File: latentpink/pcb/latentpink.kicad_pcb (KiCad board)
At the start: 6 copper layers, 97 parts, among them J1 CONN_SFP_HOST, J2 SFP_CAGE, J3 RJ45, J4 RJ45, U1 VSC8512, U2 XC7K160T-2FBG484C, U3 CY7C2245KV18-450BZXI, U4 STM32H735-UFBGA176-25, U5 DP83867, U6 DP83867, U7 BEL_FUSE_S558-5999-M8-F, U8 BEL_FUSE_S558-5999-M8-F

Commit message: Continued initial schematic capture
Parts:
- added C106: 4.7 uF, azonenberg_pcb:EIA_0603_CAP_NOSILK, F.Cu at (205.3, 132.9)
- added C110: 0.47 uF, azonenberg_pcb:EIA_0402_CAP_NOSILK, F.Cu at (208.7, 137.6)
- added C111: 0.1 uF, azonenberg_pcb:EIA_0402_CAP_NOSILK, F.Cu at (211.2, 137.2)
- added C115: 0.47 uF, azonenberg_pcb:EIA_0402_CAP_NOSILK, F.Cu at (207.4, 136.1)
- added C116: 0.47 uF, azonenberg_pcb:EIA_0402_CAP_NOSILK, F.Cu at (207.4, 134.6)
- added C119: 0.47 uF, azonenberg_pcb:EIA_0402_CAP_NOSILK, F.Cu at (208.2, 132.8)
- added C121: 0.015 uF, azonenberg_pcb:EIA_0603_CAP_NOSILK, F.Cu at (60.0, 135.2)
- added C123: 0.47 uF, azonenberg_pcb:EIA_0402_CAP_NOSILK, F.Cu at (197.5, 139.8)
- added C124: 4.7 uF, azonenberg_pcb:EIA_0603_CAP_NOSILK, F.Cu at (22.1, 62.0)
- added C125: 4.7 uF, azonenberg_pcb:EIA_0603_CAP_NOSILK, F.Cu at (22.1, 60.2)
- added C126: 4.7 uF, azonenberg_pcb:EIA_0603_CAP_NOSILK, F.Cu at (22.1, 63.8)
- added C127: 4.7 uF, azonenberg_pcb:EIA_0603_CAP_NOSILK, F.Cu at (25.4, 60.2)
- added C128: 0.47 uF, azonenberg_pcb:EIA_0402_CAP_NOSILK, F.Cu at (21.7, 68.5)
- added C129: 0.47 uF, azonenberg_pcb:EIA_0402_CAP_NOSILK, B.Cu at (29.8, 72.8)
- added C130: 0.47 uF, azonenberg_pcb:EIA_0402_CAP_NOSILK, F.Cu at (21.7, 67.0)
- added C131: 0.47 uF, azonenberg_pcb:EIA_0402_CAP_NOSILK, B.Cu at (24.8, 75.8)
- added C132: 0.47 uF, azonenberg_pcb:EIA_0402_CAP_NOSILK, F.Cu at (24.2, 65.5)
- added C133: 0.47 uF, azonenberg_pcb:EIA_0402_CAP_NOSILK, F.Cu at (30.8, 60.0)
- added C134: 0.47 uF, azonenberg_pcb:EIA_0402_CAP_NOSILK, F.Cu at (25.0, 61.9)
- added C135: 0.47 uF, azonenberg_pcb:EIA_0402_CAP_NOSILK, F.Cu at (33.3, 60.0)
- added C136: 0.47 uF, azonenberg_pcb:EIA_0402_CAP_NOSILK, F.Cu at (25.0, 63.4)
- added C137: 0.47 uF, azonenberg_pcb:EIA_0402_CAP_NOSILK, B.Cu at (31.8, 75.8)
- added C138: 0.47 uF, azonenberg_pcb:EIA_0402_CAP_NOSILK, F.Cu at (21.7, 65.5)
- added C139: 0.47 uF, azonenberg_pcb:EIA_0402_CAP_NOSILK, B.Cu at (25.8, 72.8)
- added C140: 0.47 uF, azonenberg_pcb:EIA_0402_CAP_NOSILK, B.Cu at (26.8, 72.8)
- added C141: 0.47 uF, azonenberg_pcb:EIA_0402_CAP_NOSILK, B.Cu at (24.8, 71.8)
- added C142: 0.47 uF, azonenberg_pcb:EIA_0402_CAP_NOSILK, F.Cu at (24.2, 68.5)
- added C143: 0.47 uF, azonenberg_pcb:EIA_0402_CAP_NOSILK, F.Cu at (32.5, 61.5)
- added C144: 0.47 uF, azonenberg_pcb:EIA_0402_CAP_NOSILK, B.Cu at (30.8, 72.7)
- added C145: 0.47 uF, azonenberg_pcb:EIA_0402_CAP_NOSILK, B.Cu at (27.8, 72.8)
- added C146: 0.47 uF, azonenberg_pcb:EIA_0402_CAP_NOSILK, F.Cu at (27.5, 63.4)
- added C147: 0.47 uF, azonenberg_pcb:EIA_0402_CAP_NOSILK, F.Cu at (29.2, 66.3)
- added C148: 0.47 uF, azonenberg_pcb:EIA_0402_CAP_NOSILK, F.Cu at (26.7, 66.3)
- added C149: 0.47 uF, azonenberg_pcb:EIA_0402_CAP_NOSILK, F.Cu at (24.2, 67.0)
- added C150: 0.47 uF, azonenberg_pcb:EIA_0402_CAP_NOSILK, F.Cu at (28.3, 60.0)
- added C151: 0.47 uF, azonenberg_pcb:EIA_0402_CAP_NOSILK, F.Cu at (29.2, 64.8)
- added C152: 0.47 uF, azonenberg_pcb:EIA_0402_CAP_NOSILK, B.Cu at (31.8, 71.8)
- added C153: 0.47 uF, azonenberg_pcb:EIA_0402_CAP_NOSILK, F.Cu at (27.5, 61.9)
- added C162: 4.7 uF, azonenberg_pcb:EIA_0603_CAP_NOSILK, F.Cu at (21.8, 76.5)
- added C163: 4.7 uF, azonenberg_pcb:EIA_0603_CAP_NOSILK, F.Cu at (21.8, 74.7)
- added C164: 4.7 uF, azonenberg_pcb:EIA_0603_CAP_NOSILK, F.Cu at (25.1, 76.5)
- added C165: 4.7 uF, azonenberg_pcb:EIA_0603_CAP_NOSILK, F.Cu at (25.1, 74.7)
- added C166: 4.7 uF, azonenberg_pcb:EIA_0603_CAP_NOSILK, F.Cu at (21.8, 78.3)
- added D1: GREEN, azonenberg_pcb:EIA_0603_LED, F.Cu at (202.0, 133.2)
- added D2: GREEN, azonenberg_pcb:EIA_0603_LED, F.Cu at (198.3, 133.2)
- added D3: GREEN, azonenberg_pcb:EIA_0603_LED, F.Cu at (198.3, 137.9)
- added D4: RED, azonenberg_pcb:EIA_0603_LED, F.Cu at (198.3, 135.5)
- added J10: XILINX_JTAG, azonenberg_pcb:XILINX_JTAG_PTH_MOLEX_0878311420, F.Cu at (101.0, 111.0)
- added J13: CONN_01X05, azonenberg_pcb:CONN_HEADER_2.54MM_1x5, F.Cu at (91.4, 131.3)
- added J14: CONN_01X03, azonenberg_pcb:CONN_HEADER_2.54MM_1x3, F.Cu at (83.2, 144.8)
- added J5: BEL_FUSE_0826-1G1T-23-F, azonenberg_pcb:CONN_BELFUSE_0826_1G1T_23_F, F.Cu at (44.0, 42.0)
- added J6: BARREL_JACK, azonenberg_pcb:CONN_CUI_PJ-058BH_HIPWR_BARREL_NOSLOT, F.Cu at (43.5, 136.0)
- added J7: RJ45, azonenberg_pcb:CONN_RJ45_BELSTEWART_SS-7188S-A-PG4-1-BA-xx, F.Cu at (43.7, 113.3)
- added J8: 08263-2X6R-54-F, azonenberg_pcb:CONN_RJ45_BELFUSE_0863-2X6R-54-F, F.Cu at (176.0, 108.1)
- added J9: XILINX_JTAG, azonenberg_pcb:XILINX_JTAG_PTH_MOLEX_0878311420, F.Cu at (132.0, 87.0)
- added M1: 960-27-12-D-AB-0, azonenberg_pcb:HEATSINK_WAKEFIELDVETTE_960-27-12-D-AB-0, F.Cu at (126.5, 67.5)
- added M2: 960-23-23-F-AB-0, azonenberg_pcb:HEATSINK_WAKEFIELDVETTE_960-23-23-F-AB-0, F.Cu at (81.8, 67.3)
- added M3: SCREWHOLE, azonenberg_pcb:MECHANICAL_CLEARANCEHOLE_4_40, F.Cu at (156.0, 147.0)
- added M4: SCREWHOLE, azonenberg_pcb:MECHANICAL_CLEARANCEHOLE_4_40, F.Cu at (41.0, 27.0)
- added M5: SCREWHOLE, azonenberg_pcb:MECHANICAL_CLEARANCEHOLE_4_40, F.Cu at (140.0, 30.0)
- added M6: SCREWHOLE, azonenberg_pcb:MECHANICAL_CLEARANCEHOLE_4_40, F.Cu at (47.0, 149.0)
- added R10: 4.7k, azonenberg_pcb:EIA_0402_RES_NOSILK, F.Cu at (210.7, 132.8)
- added R14: 10K, azonenberg_pcb:EIA_0402_RES_NOSILK, F.Cu at (212.4, 134.2)
- added R15: 1K, azonenberg_pcb:EIA_0402_RES_NOSILK, F.Cu at (212.4, 135.8)
- added R16: 10K, azonenberg_pcb:EIA_0402_RES_NOSILK, F.Cu at (205.0, 139.6)
- added R17: 1K, azonenberg_pcb:EIA_0402_RES_NOSILK, F.Cu at (197.5, 141.3)
- added R18: 10K, azonenberg_pcb:EIA_0402_RES_NOSILK, F.Cu at (204.9, 134.6)
- added R19: 1K, azonenberg_pcb:EIA_0402_RES_NOSILK, F.Cu at (205.0, 141.1)
- added R2: 0, azonenberg_pcb:EIA_0402_RES_NOSILK, F.Cu at (209.9, 134.2)
- added R20: 10K, azonenberg_pcb:EIA_0402_RES_NOSILK, F.Cu at (206.2, 137.6)
- added R21: 1K, azonenberg_pcb:EIA_0402_RES_NOSILK, F.Cu at (207.5, 140.6)
- added R22: 10K, azonenberg_pcb:EIA_0402_RES_NOSILK, F.Cu at (213.2, 132.8)
- added R23: 1K, azonenberg_pcb:EIA_0402_RES_NOSILK, F.Cu at (202.5, 141.1)
- added R24: 470, azonenberg_pcb:EIA_0402_RES_NOSILK, F.Cu at (202.5, 139.6)
- added R25: 470, azonenberg_pcb:EIA_0402_RES_NOSILK, F.Cu at (203.7, 138.1)
- added R26: 470, azonenberg_pcb:EIA_0402_RES_NOSILK, F.Cu at (201.2, 138.1)
- added R27: 470, azonenberg_pcb:EIA_0402_RES_NOSILK, F.Cu at (200.0, 139.8)
- added R29: 1K, azonenberg_pcb:EIA_0402_RES_NOSILK, F.Cu at (210.0, 139.1)
- added R3: 10K, azonenberg_pcb:EIA_0402_RES_NOSILK, F.Cu at (220.3, 132.8)
- added R30: 33, azonenberg_pcb:EIA_0402_RES_NOSILK, F.Cu at (220.3, 138.7)
- added R31: 1K, azonenberg_pcb:EIA_0402_RES_NOSILK, F.Cu at (207.5, 139.1)
- added R4: 10K, azonenberg_pcb:EIA_0402_RES_NOSILK, F.Cu at (222.8, 132.8)
- added R5: 10K, azonenberg_pcb:EIA_0402_RES_NOSILK, F.Cu at (200.0, 141.3)
- added R6: 0, azonenberg_pcb:EIA_0402_RES_NOSILK, F.Cu at (209.9, 135.8)
- added R7: 10K, azonenberg_pcb:EIA_0402_RES_NOSILK, F.Cu at (204.9, 136.1)
- added TP1: TESTPOINT, azonenberg_pcb:TESTPOINT_SMT_0.5MM, F.Cu at (103.4, 39.0)
- added TP2: TESTPOINT, azonenberg_pcb:TESTPOINT_SMT_0.5MM, F.Cu at (111.8, 30.2)
- added TP3: TESTPOINT, azonenberg_pcb:TESTPOINT_SMT_0.5MM, F.Cu at (219.0, 112.3)
- added TP4: TESTPOINT, azonenberg_pcb:TESTPOINT_SMT_0.5MM, F.Cu at (208.9, 122.9)
- added TP5: TESTPOINT, azonenberg_pcb:TESTPOINT_SMT_0.5MM, F.Cu at (217.5, 112.3)
- added U10: MYMGK1R812ERSR, azonenberg_pcb:MODULE_MURATA_MYMGK1R812, F.Cu at (119.5, 39.0)
- added U11: MYMGK00504ERSR, azonenberg_pcb:MODULE_MURATA_MYMGK00504ERSR, F.Cu at (95.3, 39.8)
- added U12: STM32L031-QFN32, azonenberg_pcb:QFN_32_0.5MM_5x5MM, F.Cu at (97.6, 139.2)
- added U13: MYMGK00504ERSR, azonenberg_pcb:MODULE_MURATA_MYMGK00504ERSR, F.Cu at (133.5, 100.3)
- added U14: MYMGK00504ERSR, azonenberg_pcb:MODULE_MURATA_MYMGK00504ERSR, F.Cu at (84.7, 116.6)
- added U15: MYMGK00504ERSR, azonenberg_pcb:MODULE_MURATA_MYMGK00504ERSR, F.Cu at (67.8, 116.6)
- added U16: NCP45521IMNTWG-H, azonenberg_pcb:DFN_8_0.5MM_2x2MM, F.Cu at (56.2, 134.8)
- added U17: NCP45521IMNTWG-H, azonenberg_pcb:DFN_8_0.5MM_2x2MM, F.Cu at (201.8, 135.9)
- added U9: KSZ9031RN, azonenberg_pcb:QFN_48_0.5MM_7x7MM, F.Cu at (78.8, 42.0)
- C24, C26, C32, C37, C53, C63: moved to B.Cu
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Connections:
- net /FPGA/GND renamed /QSGMII PHY/GND
- U2 pad A1: unconnected-(U2-PadA1) -> /GND
- U2 pad A12: unconnected-(U2-PadA12) -> /GND
- U2 pad A17: unconnected-(U2-PadA17) -> /1V8_IO
- U2 pad A2: unconnected-(U2-PadA2) -> /FPGA/GTX_1V2
- U2 pad A22: unconnected-(U2-PadA22) -> /GND
- U2 pad A5: unconnected-(U2-PadA5) -> /GND
- U2 pad A6: unconnected-(U2-PadA6) -> /FPGA/GTX_1V0
- U2 pad A7: unconnected-(U2-PadA7) -> /GND
- U2 pad AA12: unconnected-(U2-PadAA12) -> /GND
- U2 pad AA14: unconnected-(U2-PadAA14) -> /FPGA/QDR SRAM/QDR_D26
- U2 pad AA15: unconnected-(U2-PadAA15) -> /FPGA/QDR SRAM/QDR_BWS_2_N
- U2 pad AA16: unconnected-(U2-PadAA16) -> /FPGA/QDR SRAM/QDR_D24
- U2 pad AA17: unconnected-(U2-PadAA17) -> /1V8_IO
- U2 pad AA19: unconnected-(U2-PadAA19) -> /FPGA/QDR SRAM/QDR_D13
- U2 pad AA2: unconnected-(U2-PadAA2) -> /GND
- U2 pad AA20: unconnected-(U2-PadAA20) -> /FPGA/QDR SRAM/QDR_D11
- U2 pad AA21: unconnected-(U2-PadAA21) -> /FPGA/QDR SRAM/QDR_K_P
- U2 pad AA22: unconnected-(U2-PadAA22) -> /GND
- U2 pad AA7: unconnected-(U2-PadAA7) -> /1V8
- U2 pad AB14: unconnected-(U2-PadAB14) -> /1V8_IO
- U2 pad AB15: unconnected-(U2-PadAB15) -> /FPGA/QDR SRAM/QDR_D22
- U2 pad AB16: unconnected-(U2-PadAB16) -> /FPGA/QDR SRAM/QDR_D23
- U2 pad AB17: unconnected-(U2-PadAB17) -> /FPGA/QDR SRAM/QDR_D25
- U2 pad AB19: unconnected-(U2-PadAB19) -> /GND
- U2 pad AB20: unconnected-(U2-PadAB20) -> /FPGA/QDR SRAM/QDR_D14
- U2 pad AB21: unconnected-(U2-PadAB21) -> /FPGA/QDR SRAM/QDR_D12
- U2 pad AB22: unconnected-(U2-PadAB22) -> /FPGA/QDR SRAM/QDR_K_N
- U2 pad AB4: unconnected-(U2-PadAB4) -> /1V8
- U2 pad AB9: unconnected-(U2-PadAB9) -> /GND
- U2 pad B14: unconnected-(U2-PadB14) -> /1V8_IO
- U2 pad B19: unconnected-(U2-PadB19) -> /GND
- U2 pad B3: unconnected-(U2-PadB3) -> /GND
- U2 pad B4: unconnected-(U2-PadB4) -> /GND
- U2 pad B7: unconnected-(U2-PadB7) -> /GND
- U2 pad B9: unconnected-(U2-PadB9) -> /GND
- U2 pad C1: unconnected-(U2-PadC1) -> /GND
- U2 pad C11: unconnected-(U2-PadC11) -> /3V3
- U2 pad C16: unconnected-(U2-PadC16) -> /GND
- U2 pad C2: unconnected-(U2-PadC2) -> /FPGA/GTX_1V2
- U2 pad C21: unconnected-(U2-PadC21) -> /1V8_IO
- U2 pad C5: unconnected-(U2-PadC5) -> /GND
- U2 pad C6: unconnected-(U2-PadC6) -> /FPGA/GTX_1V0
- U2 pad C7: unconnected-(U2-PadC7) -> /GND
- U2 pad D13: unconnected-(U2-PadD13) -> /GND
- U2 pad D18: unconnected-(U2-PadD18) -> /1V8_IO
- U2 pad D3: unconnected-(U2-PadD3) -> /GND
- U2 pad D4: unconnected-(U2-PadD4) -> /GND
- U2 pad D7: unconnected-(U2-PadD7) -> /GND
- U2 pad D8: unconnected-(U2-PadD8) -> /3V3
- U2 pad E1: unconnected-(U2-PadE1) -> /GND
- U2 pad E10: unconnected-(U2-PadE10) -> /GND
- U2 pad E15: unconnected-(U2-PadE15) -> /1V8_IO
- U2 pad E2: unconnected-(U2-PadE2) -> /FPGA/GTX_1V2
- U2 pad E20: unconnected-(U2-PadE20) -> /GND
- U2 pad E21: unconnected-(U2-PadE21) -> /FPGA/QDR SRAM/QDR_A10
- U2 pad E22: unconnected-(U2-PadE22) -> /FPGA/QDR SRAM/QDR_A11
- U2 pad E5: unconnected-(U2-PadE5) -> /GND
- U2 pad E6: unconnected-(U2-PadE6) -> /FPGA/GTX_1V0
- U2 pad E7: unconnected-(U2-PadE7) -> /GND
- U2 pad F12: unconnected-(U2-PadF12) -> /3V3
- U2 pad F17: unconnected-(U2-PadF17) -> /GND
- U2 pad F19: unconnected-(U2-PadF19) -> /FPGA/QDR SRAM/QDR_A1
- U2 pad F20: unconnected-(U2-PadF20) -> /FPGA/QDR SRAM/QDR_A5
- U2 pad F21: unconnected-(U2-PadF21) -> /FPGA/QDR SRAM/QDR_A15
- U2 pad F22: unconnected-(U2-PadF22) -> /1V8_IO
- U2 pad F3: unconnected-(U2-PadF3) -> /GND
- U2 pad F4: unconnected-(U2-PadF4) -> /GND
- U2 pad F7: unconnected-(U2-PadF7) -> /GND
- U2 pad G1: unconnected-(U2-PadG1) -> /GND
- U2 pad G14: unconnected-(U2-PadG14) -> /GND
- U2 pad G18: unconnected-(U2-PadG18) -> /FPGA/QDR SRAM/QDR_A0
- U2 pad G19: unconnected-(U2-PadG19) -> /1V8_IO
- U2 pad G2: unconnected-(U2-PadG2) -> /FPGA/GTX_1V2
- U2 pad G20: unconnected-(U2-PadG20) -> /FPGA/QDR SRAM/QDR_A4
- U2 pad G21: unconnected-(U2-PadG21) -> /FPGA/QDR SRAM/QDR_A14
- U2 pad G22: unconnected-(U2-PadG22) -> /FPGA/QDR SRAM/QDR_A13
- U2 pad G5: unconnected-(U2-PadG5) -> /GND
- U2 pad G6: unconnected-(U2-PadG6) -> /FPGA/GTX_1V0
- U2 pad G9: unconnected-(U2-PadG9) -> /3V3
- U2 pad H11: unconnected-(U2-PadH11) -> /GND
- U2 pad H16: unconnected-(U2-PadH16) -> /1V8_IO
- U2 pad H18: unconnected-(U2-PadH18) -> /FPGA/QDR SRAM/QDR_RPS_N
- U2 pad H19: unconnected-(U2-PadH19) -> /FPGA/QDR SRAM/QDR_QVLD
- U2 pad H21: unconnected-(U2-PadH21) -> /GND
- U2 pad H22: unconnected-(U2-PadH22) -> /FPGA/QDR SRAM/QDR_A12
- U2 pad H3: unconnected-(U2-PadH3) -> /GND
- U2 pad H4: unconnected-(U2-PadH4) -> /GND
- U2 pad H5: unconnected-(U2-PadH5) -> /GND
- U2 pad J1: unconnected-(U2-PadJ1) -> /GND
- U2 pad J10: unconnected-(U2-PadJ10) -> /GND
- U2 pad J11: unconnected-(U2-PadJ11) -> /1V0
- U2 pad J12: unconnected-(U2-PadJ12) -> /GND
- U2 pad J13: unconnected-(U2-PadJ13) -> /1V0
- U2 pad J14: unconnected-(U2-PadJ14) -> /GND
- U2 pad J15: unconnected-(U2-PadJ15) -> /1V0
- U2 pad J18: unconnected-(U2-PadJ18) -> /GND
- U2 pad J19: unconnected-(U2-PadJ19) -> /FPGA/QDR SRAM/QDR_A3
- U2 pad J2: unconnected-(U2-PadJ2) -> /GND
- U2 pad J21: unconnected-(U2-PadJ21) -> /FPGA/QDR SRAM/QDR_A16
- U2 pad J22: unconnected-(U2-PadJ22) -> /FPGA/QDR SRAM/QDR_A17
- U2 pad J3: unconnected-(U2-PadJ3) -> /GND
- U2 pad J4: unconnected-(U2-PadJ4) -> /FPGA/GTX_1V8
- U2 pad J6: unconnected-(U2-PadJ6) -> /FPGA/FPGA_TDO
- U2 pad J7: unconnected-(U2-PadJ7) -> /1V8_IO
- U2 pad J8: unconnected-(U2-PadJ8) -> /GND
- U2 pad J9: unconnected-(U2-PadJ9) -> /1V0
- U2 pad K10: unconnected-(U2-PadK10) -> Net-(U2-PadK10)
- U2 pad K11: unconnected-(U2-PadK11) -> /GND
- U2 pad K12: unconnected-(U2-PadK12) -> Net-(U2-PadK10)
- U2 pad K13: unconnected-(U2-PadK13) -> /GND
- U2 pad K14: unconnected-(U2-PadK14) -> /1V0
- U2 pad K15: unconnected-(U2-PadK15) -> /GND
- U2 pad K16: unconnected-(U2-PadK16) -> /FPGA/QDR SRAM/QDR_WPS_N
- U2 pad K17: unconnected-(U2-PadK17) -> /FPGA/QDR SRAM/QDR_A9
- U2 pad K18: unconnected-(U2-PadK18) -> /FPGA/QDR SRAM/QDR_A2
- U2 pad K19: unconnected-(U2-PadK19) -> /FPGA/QDR SRAM/QDR_A7
- U2 pad K20: unconnected-(U2-PadK20) -> /1V8_IO
- U2 pad K5: unconnected-(U2-PadK5) -> /GND
- U2 pad K6: unconnected-(U2-PadK6) -> /FPGA/FPGA_JTAG_TDI
- U2 pad K7: unconnected-(U2-PadK7) -> /FPGA/FPGA_JTAG_TCK
- U2 pad K8: unconnected-(U2-PadK8) -> /1V0
- U2 pad K9: unconnected-(U2-PadK9) -> /GND
- U2 pad L10: unconnected-(U2-PadL10) -> /GND
- U2 pad L13: unconnected-(U2-PadL13) -> /1V0
- U2 pad L14: unconnected-(U2-PadL14) -> /GND
- U2 pad L15: unconnected-(U2-PadL15) -> /1V0
- U2 pad L16: unconnected-(U2-PadL16) -> /FPGA/QDR SRAM/QDR_A8
- U2 pad L17: unconnected-(U2-PadL17) -> /1V8_IO
- U2 pad L18: unconnected-(U2-PadL18) -> /FPGA/QDR SRAM/QDR_A6
- U2 pad L19: unconnected-(U2-PadL19) -> /FPGA/QDR SRAM/QDR_CQ_P
- U2 pad L2: unconnected-(U2-PadL2) -> /GND
- U2 pad L20: unconnected-(U2-PadL20) -> /FPGA/QDR SRAM/QDR_CQ_N
- U2 pad L22: unconnected-(U2-PadL22) -> /GND
- U2 pad L6: unconnected-(U2-PadL6) -> /FPGA/FPGA_JTAG_TMS
- U2 pad L8: unconnected-(U2-PadL8) -> /GND
- U2 pad L9: unconnected-(U2-PadL9) -> /1V0
- U2 pad M10: unconnected-(U2-PadM10) -> Net-(U2-PadK10)
- U2 pad M13: unconnected-(U2-PadM13) -> /GND
- U2 pad M14: unconnected-(U2-PadM14) -> /1V0
- U2 pad M15: unconnected-(U2-PadM15) -> /GND
- U2 pad M17: unconnected-(U2-PadM17) -> /FPGA/QDR SRAM/QDR_A20
- U2 pad M18: unconnected-(U2-PadM18) -> /FPGA/QDR SRAM/QDR_A19
- U2 pad M19: unconnected-(U2-PadM19) -> /GND
- U2 pad M4: unconnected-(U2-PadM4) -> /1V8
- U2 pad M8: unconnected-(U2-PadM8) -> /1V0
- U2 pad M9: unconnected-(U2-PadM9) -> /GND
- U2 pad N1: unconnected-(U2-PadN1) -> /1V8
- U2 pad N10: unconnected-(U2-PadN10) -> /GND
- U2 pad N13: unconnected-(U2-PadN13) -> /1V0
- U2 pad N14: unconnected-(U2-PadN14) -> /GND
- U2 pad N15: unconnected-(U2-PadN15) -> /1V0
- U2 pad N16: unconnected-(U2-PadN16) -> /GND
- U2 pad N18: unconnected-(U2-PadN18) -> /FPGA/QDR SRAM/QDR_SYSCLK_P
- U2 pad N19: unconnected-(U2-PadN19) -> /FPGA/QDR SRAM/QDR_SYSCLK_N
- U2 pad N21: unconnected-(U2-PadN21) -> /1V8_IO
- U2 pad N22: unconnected-(U2-PadN22) -> /FPGA/QDR SRAM/QDR_A18
- U2 pad N6: unconnected-(U2-PadN6) -> /GND
- U2 pad N7: unconnected-(U2-PadN7) -> /1V8_IO
- U2 pad N8: unconnected-(U2-PadN8) -> /GND
- U2 pad N9: unconnected-(U2-PadN9) -> /1V0
- U2 pad P10: unconnected-(U2-PadP10) -> Net-(U2-PadK10)
- U2 pad P11: unconnected-(U2-PadP11) -> /GND
- U2 pad P12: unconnected-(U2-PadP12) -> Net-(U2-PadK10)
- U2 pad P13: unconnected-(U2-PadP13) -> /GND
- U2 pad P14: unconnected-(U2-PadP14) -> /1V0
- U2 pad P15: unconnected-(U2-PadP15) -> /GND
- U2 pad P18: unconnected-(U2-PadP18) -> /1V8_IO
- U2 pad P3: unconnected-(U2-PadP3) -> /GND
- U2 pad P8: unconnected-(U2-PadP8) -> Net-(U2-PadK10)
- U2 pad P9: unconnected-(U2-PadP9) -> /GND
- U2 pad R10: unconnected-(U2-PadR10) -> /GND
- U2 pad R11: unconnected-(U2-PadR11) -> Net-(U2-PadK10)
- U2 pad R12: unconnected-(U2-PadR12) -> /GND
- U2 pad R13: unconnected-(U2-PadR13) -> /1V0
- U2 pad R14: unconnected-(U2-PadR14) -> /GND
- U2 pad R15: unconnected-(U2-PadR15) -> /1V0
- U2 pad R16: unconnected-(U2-PadR16) -> /FPGA/QDR SRAM/QDR_D29
- U2 pad R20: unconnected-(U2-PadR20) -> /GND
- U2 pad R5: unconnected-(U2-PadR5) -> /1V8
- U2 pad R8: unconnected-(U2-PadR8) -> /GND
- U2 pad R9: unconnected-(U2-PadR9) -> Net-(U2-PadK10)
- U2 pad T12: unconnected-(U2-PadT12) -> /1V8
- U2 pad T15: unconnected-(U2-PadT15) -> /FPGA/QDR SRAM/QDR_D35
- U2 pad T16: unconnected-(U2-PadT16) -> /FPGA/QDR SRAM/QDR_D30
- U2 pad T17: unconnected-(U2-PadT17) -> /GND
- U2 pad T2: unconnected-(U2-PadT2) -> /1V8
- U2 pad T20: unconnected-(U2-PadT20) -> /FPGA/QDR SRAM/QDR_D8
- U2 pad T21: unconnected-(U2-PadT21) -> /FPGA/QDR SRAM/QDR_D0
- U2 pad T22: unconnected-(U2-PadT22) -> /1V8_IO
- U2 pad T7: unconnected-(U2-PadT7) -> /GND
- U2 pad U14: unconnected-(U2-PadU14) -> /GND
- U2 pad U15: unconnected-(U2-PadU15) -> /FPGA/QDR SRAM/QDR_BWS_3_N
- U2 pad U16: unconnected-(U2-PadU16) -> /FPGA/QDR SRAM/QDR_D27
- U2 pad U17: unconnected-(U2-PadU17) -> /FPGA/QDR SRAM/QDR_D6
- U2 pad U19: unconnected-(U2-PadU19) -> /1V8_IO
- U2 pad U20: unconnected-(U2-PadU20) -> /FPGA/QDR SRAM/QDR_BWS_0_N
- U2 pad U21: unconnected-(U2-PadU21) -> /FPGA/QDR SRAM/QDR_D1
- U2 pad U22: unconnected-(U2-PadU22) -> /FPGA/QDR SRAM/QDR_D2
- U2 pad U4: unconnected-(U2-PadU4) -> /GND
- U2 pad U9: unconnected-(U2-PadU9) -> /1V8
- U2 pad V1: unconnected-(U2-PadV1) -> /GND
- U2 pad V11: unconnected-(U2-PadV11) -> /GND
- U2 pad V15: unconnected-(U2-PadV15) -> /FPGA/QDR SRAM/QDR_D33
- U2 pad V16: unconnected-(U2-PadV16) -> /1V8_IO
- U2 pad V17: unconnected-(U2-PadV17) -> /FPGA/QDR SRAM/QDR_D28
- U2 pad V18: unconnected-(U2-PadV18) -> /FPGA/QDR SRAM/QDR_D7
- U2 pad V19: unconnected-(U2-PadV19) -> /FPGA/QDR SRAM/QDR_D17
- U2 pad V20: unconnected-(U2-PadV20) -> /FPGA/QDR SRAM/QDR_D15
- U2 pad V21: unconnected-(U2-PadV21) -> /GND
- U2 pad V22: unconnected-(U2-PadV22) -> /FPGA/QDR SRAM/QDR_D3
- U2 pad V6: unconnected-(U2-PadV6) -> /1V8
- U2 pad W13: unconnected-(U2-PadW13) -> /1V8
- U2 pad W14: unconnected-(U2-PadW14) -> /FPGA/QDR SRAM/QDR_D31
- U2 pad W15: unconnected-(U2-PadW15) -> /FPGA/QDR SRAM/QDR_D34
- U2 pad W17: unconnected-(U2-PadW17) -> /FPGA/QDR SRAM/QDR_D20
- U2 pad W18: unconnected-(U2-PadW18) -> /GND
- U2 pad W19: unconnected-(U2-PadW19) -> /FPGA/QDR SRAM/QDR_BWS_1_N
- U2 pad W20: unconnected-(U2-PadW20) -> /FPGA/QDR SRAM/QDR_D16
- U2 pad W21: unconnected-(U2-PadW21) -> /FPGA/QDR SRAM/QDR_D4
- U2 pad W22: unconnected-(U2-PadW22) -> /FPGA/QDR SRAM/QDR_D5
- U2 pad W3: unconnected-(U2-PadW3) -> /1V8
- U2 pad W8: unconnected-(U2-PadW8) -> /GND
- U2 pad Y10: unconnected-(U2-PadY10) -> /1V8
- U2 pad Y14: unconnected-(U2-PadY14) -> /FPGA/QDR SRAM/QDR_D32
- U2 pad Y15: unconnected-(U2-PadY15) -> /GND
- U2 pad Y17: unconnected-(U2-PadY17) -> /FPGA/QDR SRAM/QDR_D21
- U2 pad Y18: unconnected-(U2-PadY18) -> /FPGA/QDR SRAM/QDR_D18
- U2 pad Y19: unconnected-(U2-PadY19) -> /FPGA/QDR SRAM/QDR_D19
- U2 pad Y20: unconnected-(U2-PadY20) -> /1V8_IO
- U2 pad Y21: unconnected-(U2-PadY21) -> /FPGA/QDR SRAM/QDR_D9
- U2 pad Y22: unconnected-(U2-PadY22) -> /FPGA/QDR SRAM/QDR_D10
- U2 pad Y5: unconnected-(U2-PadY5) -> /GND
- U3 pad A1: unconnected-(U3-PadA1) -> /FPGA/QDR SRAM/QDR_CQ_N
- U3 pad A10: unconnected-(U3-PadA10) -> /FPGA/QDR SRAM/QDR_A19
- U3 pad A11: unconnected-(U3-PadA11) -> /FPGA/QDR SRAM/QDR_CQ_P
- U3 pad A2: unconnected-(U3-PadA2) -> /FPGA/QDR SRAM/QDR_A20
- U3 pad A3: unconnected-(U3-PadA3) -> /FPGA/QDR SRAM/QDR_A18
- U3 pad A4: unconnected-(U3-PadA4) -> /FPGA/QDR SRAM/QDR_WPS_N
- U3 pad A5: unconnected-(U3-PadA5) -> /FPGA/QDR SRAM/QDR_BWS_2_N
- U3 pad A6: unconnected-(U3-PadA6) -> /FPGA/QDR SRAM/QDR_K_N
- U3 pad A7: unconnected-(U3-PadA7) -> /FPGA/QDR SRAM/QDR_BWS_1_N
- U3 pad A8: unconnected-(U3-PadA8) -> /FPGA/QDR SRAM/QDR_RPS_N
- U3 pad A9: unconnected-(U3-PadA9) -> /FPGA/QDR SRAM/QDR_A0
- U3 pad B3: unconnected-(U3-PadB3) -> /FPGA/QDR SRAM/QDR_D18
- U3 pad B4: unconnected-(U3-PadB4) -> /FPGA/QDR SRAM/QDR_A1
- U3 pad B5: unconnected-(U3-PadB5) -> /FPGA/QDR SRAM/QDR_BWS_3_N
- U3 pad B6: unconnected-(U3-PadB6) -> /FPGA/QDR SRAM/QDR_K_P
- U3 pad B7: unconnected-(U3-PadB7) -> /FPGA/QDR SRAM/QDR_BWS_0_N
- U3 pad B8: unconnected-(U3-PadB8) -> /FPGA/QDR SRAM/QDR_A2
- U3 pad B9: unconnected-(U3-PadB9) -> /FPGA/QDR SRAM/QDR_D17
- U3 pad C1: unconnected-(U3-PadC1) -> /FPGA/QDR SRAM/QDR_D27
- U3 pad C11: unconnected-(U3-PadC11) -> /FPGA/QDR SRAM/QDR_D8
- U3 pad C3: unconnected-(U3-PadC3) -> /FPGA/QDR SRAM/QDR_D19
- U3 pad C4: unconnected-(U3-PadC4) -> /GND
- U3 pad C5: unconnected-(U3-PadC5) -> /FPGA/QDR SRAM/QDR_A3
- U3 pad C7: unconnected-(U3-PadC7) -> /FPGA/QDR SRAM/QDR_A4
- U3 pad C8: unconnected-(U3-PadC8) -> /GND
- U3 pad C9: unconnected-(U3-PadC9) -> /FPGA/QDR SRAM/QDR_D16
- U3 pad D1: unconnected-(U3-PadD1) -> /FPGA/QDR SRAM/QDR_D28
- U3 pad D10: unconnected-(U3-PadD10) -> /FPGA/QDR SRAM/QDR_D15
- U3 pad D11: unconnected-(U3-PadD11) -> /FPGA/QDR SRAM/QDR_D7
- U3 pad D2: unconnected-(U3-PadD2) -> /FPGA/QDR SRAM/QDR_D20
- U3 pad D4: unconnected-(U3-PadD4) -> /GND
- U3 pad D5: unconnected-(U3-PadD5) -> /GND
- U3 pad D6: unconnected-(U3-PadD6) -> /GND
- U3 pad D7: unconnected-(U3-PadD7) -> /GND
- U3 pad D8: unconnected-(U3-PadD8) -> /GND
- U3 pad E10: unconnected-(U3-PadE10) -> /FPGA/QDR SRAM/QDR_D6
- U3 pad E2: unconnected-(U3-PadE2) -> /FPGA/QDR SRAM/QDR_D29
- U3 pad E4: unconnected-(U3-PadE4) -> /1V8_IO
- U3 pad E5: unconnected-(U3-PadE5) -> /GND
- U3 pad E6: unconnected-(U3-PadE6) -> /GND
- U3 pad E7: unconnected-(U3-PadE7) -> /GND
- U3 pad E8: unconnected-(U3-PadE8) -> /1V8_IO
- U3 pad F3: unconnected-(U3-PadF3) -> /FPGA/QDR SRAM/QDR_D21
- U3 pad F4: unconnected-(U3-PadF4) -> /1V8_IO
- U3 pad F5: unconnected-(U3-PadF5) -> /1V8
- U3 pad F6: unconnected-(U3-PadF6) -> /GND
- U3 pad F7: unconnected-(U3-PadF7) -> /1V8
- U3 pad F8: unconnected-(U3-PadF8) -> /1V8_IO
- U3 pad F9: unconnected-(U3-PadF9) -> /FPGA/QDR SRAM/QDR_D14
- U3 pad G1: unconnected-(U3-PadG1) -> /FPGA/QDR SRAM/QDR_D30
- U3 pad G10: unconnected-(U3-PadG10) -> /FPGA/QDR SRAM/QDR_D13
- U3 pad G11: unconnected-(U3-PadG11) -> /FPGA/QDR SRAM/QDR_D5
- U3 pad G2: unconnected-(U3-PadG2) -> /FPGA/QDR SRAM/QDR_D22
- U3 pad G4: unconnected-(U3-PadG4) -> /1V8_IO
- U3 pad G5: unconnected-(U3-PadG5) -> /1V8
- U3 pad G6: unconnected-(U3-PadG6) -> /GND
- U3 pad G7: unconnected-(U3-PadG7) -> /1V8
- U3 pad G8: unconnected-(U3-PadG8) -> /1V8_IO
- U3 pad H3: unconnected-(U3-PadH3) -> /1V8_IO
- U3 pad H4: unconnected-(U3-PadH4) -> /1V8_IO
- U3 pad H5: unconnected-(U3-PadH5) -> /1V8
- U3 pad H6: unconnected-(U3-PadH6) -> /GND
- U3 pad H7: unconnected-(U3-PadH7) -> /1V8
- U3 pad H8: unconnected-(U3-PadH8) -> /1V8_IO
- U3 pad H9: unconnected-(U3-PadH9) -> /1V8_IO
- U3 pad J1: unconnected-(U3-PadJ1) -> /FPGA/QDR SRAM/QDR_D31
- U3 pad J11: unconnected-(U3-PadJ11) -> /FPGA/QDR SRAM/QDR_D4
- U3 pad J3: unconnected-(U3-PadJ3) -> /FPGA/QDR SRAM/QDR_D23
- U3 pad J4: unconnected-(U3-PadJ4) -> /1V8_IO
- U3 pad J5: unconnected-(U3-PadJ5) -> /1V8
- U3 pad J6: unconnected-(U3-PadJ6) -> /GND
- U3 pad J7: unconnected-(U3-PadJ7) -> /1V8
- U3 pad J8: unconnected-(U3-PadJ8) -> /1V8_IO
- U3 pad J9: unconnected-(U3-PadJ9) -> /FPGA/QDR SRAM/QDR_D12
- U3 pad K10: unconnected-(U3-PadK10) -> /FPGA/QDR SRAM/QDR_D3
- U3 pad K2: unconnected-(U3-PadK2) -> /FPGA/QDR SRAM/QDR_D32
- U3 pad K4: unconnected-(U3-PadK4) -> /1V8_IO
- U3 pad K5: unconnected-(U3-PadK5) -> /1V8
- U3 pad K6: unconnected-(U3-PadK6) -> /GND
- U3 pad K7: unconnected-(U3-PadK7) -> /1V8
- U3 pad K8: unconnected-(U3-PadK8) -> /1V8_IO
- U3 pad L3: unconnected-(U3-PadL3) -> /FPGA/QDR SRAM/QDR_D24
- U3 pad L4: unconnected-(U3-PadL4) -> /1V8_IO
- U3 pad L5: unconnected-(U3-PadL5) -> /GND
- U3 pad L6: unconnected-(U3-PadL6) -> /GND
- U3 pad L7: unconnected-(U3-PadL7) -> /GND
- U3 pad L8: unconnected-(U3-PadL8) -> /1V8_IO
- U3 pad L9: unconnected-(U3-PadL9) -> /FPGA/QDR SRAM/QDR_D11
- U3 pad M1: unconnected-(U3-PadM1) -> /FPGA/QDR SRAM/QDR_D33
- U3 pad M11: unconnected-(U3-PadM11) -> /FPGA/QDR SRAM/QDR_D2
- U3 pad M3: unconnected-(U3-PadM3) -> /FPGA/QDR SRAM/QDR_D25
- U3 pad M4: unconnected-(U3-PadM4) -> /GND
- U3 pad M5: unconnected-(U3-PadM5) -> /GND
- U3 pad M6: unconnected-(U3-PadM6) -> /GND
- U3 pad M7: unconnected-(U3-PadM7) -> /GND
- U3 pad M8: unconnected-(U3-PadM8) -> /GND
- U3 pad M9: unconnected-(U3-PadM9) -> /FPGA/QDR SRAM/QDR_D10
- U3 pad N1: unconnected-(U3-PadN1) -> /FPGA/QDR SRAM/QDR_D34
- U3 pad N10: unconnected-(U3-PadN10) -> /FPGA/QDR SRAM/QDR_D9
- U3 pad N11: unconnected-(U3-PadN11) -> /FPGA/QDR SRAM/QDR_D1
- U3 pad N2: unconnected-(U3-PadN2) -> /FPGA/QDR SRAM/QDR_D26
- U3 pad N4: unconnected-(U3-PadN4) -> /GND
- U3 pad N5: unconnected-(U3-PadN5) -> /FPGA/QDR SRAM/QDR_A5
- U3 pad N6: unconnected-(U3-PadN6) -> /FPGA/QDR SRAM/QDR_A6
- U3 pad N7: unconnected-(U3-PadN7) -> /FPGA/QDR SRAM/QDR_A7
- U3 pad N8: unconnected-(U3-PadN8) -> /GND
- U3 pad P10: unconnected-(U3-PadP10) -> /FPGA/QDR SRAM/QDR_D0
- U3 pad P2: unconnected-(U3-PadP2) -> /FPGA/QDR SRAM/QDR_D35
- U3 pad P4: unconnected-(U3-PadP4) -> /FPGA/QDR SRAM/QDR_A8
- U3 pad P5: unconnected-(U3-PadP5) -> /FPGA/QDR SRAM/QDR_A9
- U3 pad P6: unconnected-(U3-PadP6) -> /FPGA/QDR SRAM/QDR_QVLD
- U3 pad P7: unconnected-(U3-PadP7) -> /FPGA/QDR SRAM/QDR_A10
- U3 pad P8: unconnected-(U3-PadP8) -> /FPGA/QDR SRAM/QDR_A11
- U3 pad R3: unconnected-(U3-PadR3) -> /FPGA/QDR SRAM/QDR_A12
- U3 pad R4: unconnected-(U3-PadR4) -> /FPGA/QDR SRAM/QDR_A13
- U3 pad R5: unconnected-(U3-PadR5) -> /FPGA/QDR SRAM/QDR_A14
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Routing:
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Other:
- board outline added: 145 x 134 mm
- copper layers 6 -> 8

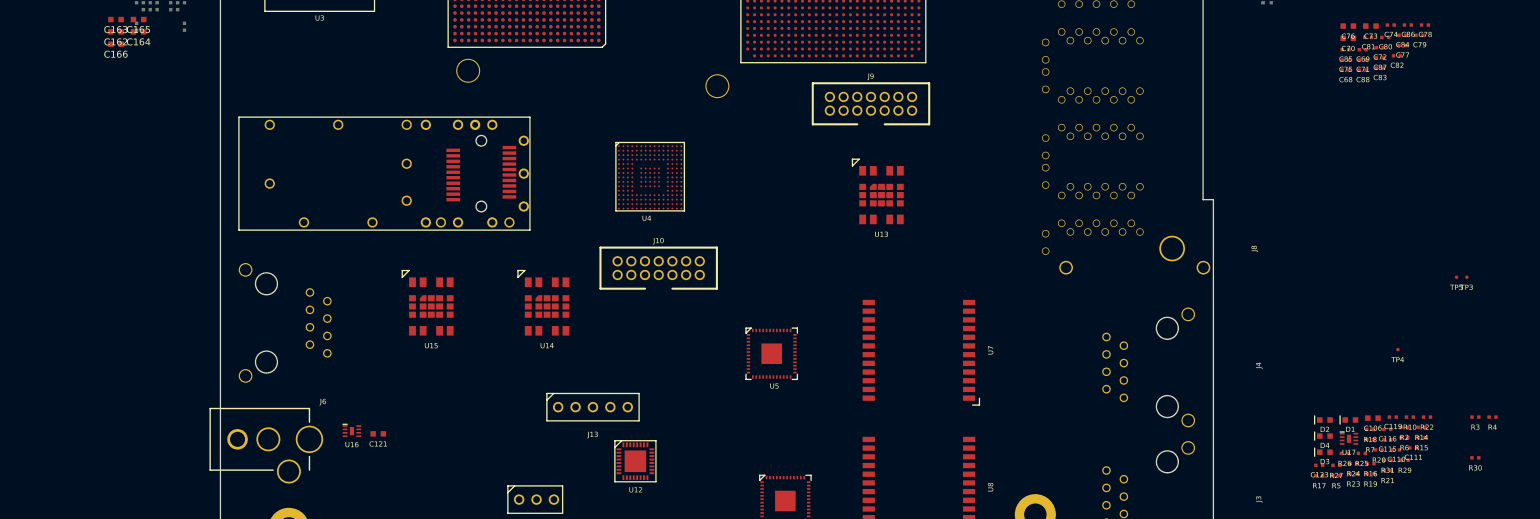
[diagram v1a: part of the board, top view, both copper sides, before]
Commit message: Continued work on schematic, mostly power supply and QDR
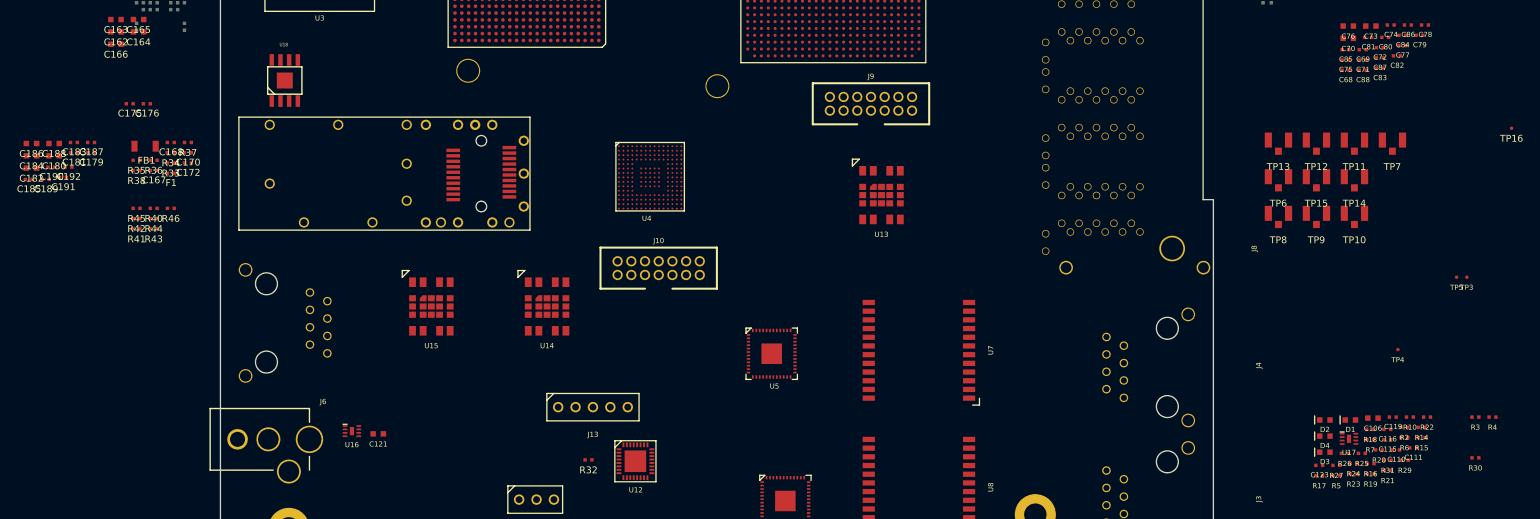
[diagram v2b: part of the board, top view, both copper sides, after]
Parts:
- added C167: 0.1 uF, azonenberg_pcb:EIA_0402_CAP_NOSILK, F.Cu at (27.2, 96.8)
- added C168: 0.1 uF, azonenberg_pcb:EIA_0402_CAP_NOSILK, F.Cu at (29.8, 92.7)
- added C170: 0.47 uF, azonenberg_pcb:EIA_0402_CAP_NOSILK, F.Cu at (32.2, 94.2)
- added C172: 0.47 uF, azonenberg_pcb:EIA_0402_CAP_NOSILK, F.Cu at (32.2, 95.7)
- added C175: 0.47 uF, azonenberg_pcb:EIA_0402_CAP_NOSILK, F.Cu at (23.8, 87.0)
- added C176: 0.47 uF, azonenberg_pcb:EIA_0402_CAP_NOSILK, F.Cu at (26.2, 87.0)
- added C179: 0.47 uF, azonenberg_pcb:EIA_0402_CAP_NOSILK, F.Cu at (18.1, 94.2)
- added C180: 4.7 uF, azonenberg_pcb:EIA_0603_CAP_NOSILK, F.Cu at (12.7, 94.6)
- added C181: 0.47 uF, azonenberg_pcb:EIA_0402_CAP_NOSILK, F.Cu at (15.6, 94.2)
- added C182: 4.7 uF, azonenberg_pcb:EIA_0603_CAP_NOSILK, F.Cu at (9.41, 96.4)
- added C183: 0.47 uF, azonenberg_pcb:EIA_0402_CAP_NOSILK, F.Cu at (15.6, 92.7)
- added C184: 4.7 uF, azonenberg_pcb:EIA_0603_CAP_NOSILK, F.Cu at (9.41, 94.6)
- added C185: 0.47 uF, azonenberg_pcb:EIA_0402_CAP_NOSILK, F.Cu at (9.01, 98.0)
- added C186: 4.7 uF, azonenberg_pcb:EIA_0603_CAP_NOSILK, F.Cu at (9.41, 92.8)
- added C187: 0.47 uF, azonenberg_pcb:EIA_0402_CAP_NOSILK, F.Cu at (18.1, 92.7)
- added C188: 4.7 uF, azonenberg_pcb:EIA_0603_CAP_NOSILK, F.Cu at (12.7, 92.8)
- added C189: 0.47 uF, azonenberg_pcb:EIA_0402_CAP_NOSILK, F.Cu at (11.5, 98.0)
- added C190: 0.47 uF, azonenberg_pcb:EIA_0402_CAP_NOSILK, F.Cu at (12.3, 96.2)
- added C191: 0.47 uF, azonenberg_pcb:EIA_0402_CAP_NOSILK, F.Cu at (14.0, 97.8)
- added C192: 0.47 uF, azonenberg_pcb:EIA_0402_CAP_NOSILK, F.Cu at (14.8, 96.2)
- added F1: ERB-RD4R00X, azonenberg_pcb:EIA_0402_CAP_NOSILK, F.Cu at (29.8, 97.2)
- added FB1: BLM31KN271SN1L, azonenberg_pcb:EIA_1206_CAP_NOSILK, F.Cu at (26.0, 93.2)
- added R32: 1K, azonenberg_pcb:EIA_0402_RES_NOSILK, F.Cu at (90.8, 139.0)
- added R33: 0, azonenberg_pcb:EIA_0402_RES_NOSILK, F.Cu at (29.8, 95.7)
- added R34: 0, azonenberg_pcb:EIA_0402_RES_NOSILK, F.Cu at (29.8, 94.2)
- added R35: 0, azonenberg_pcb:EIA_0402_RES_NOSILK, F.Cu at (24.8, 95.2)
- added R36: 0, azonenberg_pcb:EIA_0402_RES_NOSILK, F.Cu at (27.2, 95.2)
- added R37: 0, azonenberg_pcb:EIA_0402_RES_NOSILK, F.Cu at (32.2, 92.7)
- added R38: 0, azonenberg_pcb:EIA_0402_RES_NOSILK, F.Cu at (24.8, 96.8)
- added R40: 330, azonenberg_pcb:EIA_0402_RES_NOSILK, F.Cu at (27.2, 102.3)
- added R41: 4.7K, azonenberg_pcb:EIA_0402_RES_NOSILK, F.Cu at (24.8, 105.3)
- added R42: 4.7K, azonenberg_pcb:EIA_0402_RES_NOSILK, F.Cu at (24.8, 103.8)
- added R43: 33, azonenberg_pcb:EIA_0402_RES_NOSILK, F.Cu at (27.2, 105.3)
- added R44: 0, azonenberg_pcb:EIA_0402_RES_NOSILK, F.Cu at (27.2, 103.8)
- added R45: 0, azonenberg_pcb:EIA_0402_RES_NOSILK, F.Cu at (24.8, 102.3)
- added R46: 0, azonenberg_pcb:EIA_0402_RES_NOSILK, F.Cu at (29.8, 102.3)
- added TP10: U.FL, azonenberg_pcb:CONN_U.FL_TE_1909763-1, F.Cu at (202.6, 103.1)
- added TP11: U.FL, azonenberg_pcb:CONN_U.FL_TE_1909763-1, F.Cu at (202.6, 92.4)
- added TP12: U.FL, azonenberg_pcb:CONN_U.FL_TE_1909763-1, F.Cu at (197.1, 92.4)
- added TP13: U.FL, azonenberg_pcb:CONN_U.FL_TE_1909763-1, F.Cu at (191.5, 92.4)
- added TP14: U.FL, azonenberg_pcb:CONN_U.FL_TE_1909763-1, F.Cu at (202.6, 97.8)
- added TP15: U.FL, azonenberg_pcb:CONN_U.FL_TE_1909763-1, F.Cu at (197.1, 97.8)
- added TP16: TESTPOINT, azonenberg_pcb:TESTPOINT_SMT_0.5MM, F.Cu at (225.5, 90.6)
- added TP6: U.FL, azonenberg_pcb:CONN_U.FL_TE_1909763-1, F.Cu at (191.5, 97.8)
- added TP7: U.FL, azonenberg_pcb:CONN_U.FL_TE_1909763-1, F.Cu at (208.2, 92.4)
- added TP8: U.FL, azonenberg_pcb:CONN_U.FL_TE_1909763-1, F.Cu at (191.5, 103.1)
- added TP9: U.FL, azonenberg_pcb:CONN_U.FL_TE_1909763-1, F.Cu at (197.1, 103.1)
- added U18: LP2996AMRE, azonenberg_pcb:SOIC_8_3.9MM_EPAD, F.Cu at (46.4, 83.6)
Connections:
- net /Power Supply/3V3_SB renamed /3V3_SB
- U10 pad 15: /1V0 -> /Power Supply/1V0_RAW
- U10 pad 16: /1V0 -> /Power Supply/1V0_RAW
- U10 pad 17: /1V0 -> /Power Supply/1V0_RAW
- U10 pad 18: /1V0 -> /Power Supply/1V0_RAW
- U10 pad 19: /1V0 -> /Power Supply/1V0_RAW
- U10 pad 20: /1V0 -> /Power Supply/1V0_RAW
- U10 pad 21: /1V0 -> /Power Supply/1V0_SENSE
- U11 pad 6: /1V2 -> /Power Supply/1V2_RAW
- U11 pad 7: /1V2 -> /Power Supply/1V2_RAW
- U12 pad 2: unconnected-(U12-Pad2) -> /Power Supply/VTT_EN
- U13 pad 6: /2V5 -> /Power Supply/2V5_RAW
- U13 pad 7: /2V5 -> /Power Supply/2V5_RAW
- U14 pad 6: /3V3 -> /Power Supply/3V3_RAW
- U14 pad 7: /3V3 -> /Power Supply/3V3_RAW
- U15 pad 6: /1V8 -> /Power Supply/1V8_RAW
- U15 pad 7: /1V8 -> /Power Supply/1V8_RAW
- U2 pad A13: unconnected-(U2-PadA13) -> /FPGA/QDR SRAM/QDR_Q4
- U2 pad A14: unconnected-(U2-PadA14) -> /FPGA/QDR SRAM/QDR_Q5
- U2 pad A16: unconnected-(U2-PadA16) -> /FPGA/QDR SRAM/QDR_Q12
- U2 pad A18: unconnected-(U2-PadA18) -> /FPGA/QDR SRAM/QDR_Q14
- U2 pad A19: unconnected-(U2-PadA19) -> /FPGA/QDR SRAM/QDR_Q29
- U2 pad A20: unconnected-(U2-PadA20) -> /FPGA/QDR SRAM/QDR_Q30
- U2 pad A21: unconnected-(U2-PadA21) -> /FPGA/QDR SRAM/QDR_Q31
- U2 pad AA7: /1V8 -> /1V8_IO
- U2 pad AB4: /1V8 -> /1V8_IO
- U2 pad B12: unconnected-(U2-PadB12) -> /FPGA/QDR SRAM/QDR_Q3
- U2 pad B13: unconnected-(U2-PadB13) -> /FPGA/QDR SRAM/QDR_Q7
- U2 pad B16: unconnected-(U2-PadB16) -> /FPGA/QDR SRAM/QDR_Q11
- U2 pad B17: unconnected-(U2-PadB17) -> /FPGA/QDR SRAM/QDR_Q13
- U2 pad B18: unconnected-(U2-PadB18) -> /FPGA/QDR SRAM/QDR_Q28
- U2 pad B20: unconnected-(U2-PadB20) -> /FPGA/QDR SRAM/QDR_Q34
- U2 pad B21: unconnected-(U2-PadB21) -> /FPGA/QDR SRAM/QDR_Q35
- U2 pad C12: unconnected-(U2-PadC12) -> /FPGA/QDR SRAM/QDR_Q2
- U2 pad C13: unconnected-(U2-PadC13) -> /FPGA/QDR SRAM/QDR_Q6
- U2 pad C14: unconnected-(U2-PadC14) -> /FPGA/QDR SRAM/QDR_Q9
- U2 pad C15: unconnected-(U2-PadC15) -> /FPGA/QDR SRAM/QDR_Q10
- U2 pad C17: unconnected-(U2-PadC17) -> /FPGA/QDR SRAM/QDR_Q17
- U2 pad C19: unconnected-(U2-PadC19) -> /FPGA/QDR SRAM/QDR_Q27
- U2 pad C20: unconnected-(U2-PadC20) -> /QDR_VREF
- U2 pad D14: unconnected-(U2-PadD14) -> /QDR_VREF
- U2 pad D15: unconnected-(U2-PadD15) -> /FPGA/QDR SRAM/QDR_Q15
- U2 pad D16: unconnected-(U2-PadD16) -> /FPGA/QDR SRAM/QDR_Q16
- U2 pad D17: unconnected-(U2-PadD17) -> /FPGA/QDR SRAM/QDR_Q21
- U2 pad D19: unconnected-(U2-PadD19) -> /FPGA/QDR SRAM/QDR_Q26
- U2 pad D21: unconnected-(U2-PadD21) -> /FPGA/QDR SRAM/QDR_Q32
- U2 pad D22: unconnected-(U2-PadD22) -> /FPGA/QDR SRAM/QDR_Q33
- U2 pad E14: unconnected-(U2-PadE14) -> /FPGA/QDR SRAM/QDR_Q8
- U2 pad E16: unconnected-(U2-PadE16) -> /FPGA/QDR SRAM/QDR_Q20
- U2 pad E17: unconnected-(U2-PadE17) -> /FPGA/QDR SRAM/QDR_Q18
- U2 pad E18: unconnected-(U2-PadE18) -> /FPGA/QDR SRAM/QDR_Q19
- U2 pad E19: unconnected-(U2-PadE19) -> /FPGA/QDR SRAM/QDR_Q25
- U2 pad F18: unconnected-(U2-PadF18) -> /FPGA/QDR SRAM/QDR_Q24
- U2 pad G15: unconnected-(U2-PadG15) -> /FPGA/QDR SRAM/QDR_Q0
- U2 pad G16: unconnected-(U2-PadG16) -> /FPGA/QDR SRAM/QDR_Q1
- U2 pad G7: unconnected-(U2-PadG7) -> Net-(U2-PadG7)
- U2 pad H6: unconnected-(U2-PadH6) -> Net-(U2-PadH6)
- U2 pad H7: unconnected-(U2-PadH7) -> Net-(U2-PadH7)
- U2 pad J16: unconnected-(U2-PadJ16) -> /FPGA/QDR SRAM/QDR_Q22
- U2 pad J17: unconnected-(U2-PadJ17) -> /FPGA/QDR SRAM/QDR_Q23
- U2 pad J5: unconnected-(U2-PadJ5) -> Net-(U2-PadJ5)
- U2 pad K10: Net-(U2-PadK10) -> /1V8
- U2 pad K12: Net-(U2-PadK10) -> /1V8
- U2 pad K21: unconnected-(U2-PadK21) -> /FPGA/QDR SRAM/QDR_ODT
- U2 pad L11: unconnected-(U2-PadL11) -> /GND
- U2 pad L12: unconnected-(U2-PadL12) -> /GND
- U2 pad L7: unconnected-(U2-PadL7) -> /FPGA/FPGA_INIT
- U2 pad M10: Net-(U2-PadK10) -> /1V8
- U2 pad M11: unconnected-(U2-PadM11) -> /GND
- U2 pad M12: unconnected-(U2-PadM12) -> /GND
- U2 pad M4: /1V8 -> /1V8_IO
- U2 pad M6: unconnected-(U2-PadM6) -> /FPGA/FPGA_RST_N
- U2 pad M7: unconnected-(U2-PadM7) -> /GND
- U2 pad N1: /1V8 -> /1V8_IO
- U2 pad N11: unconnected-(U2-PadN11) -> /GND
- U2 pad N12: unconnected-(U2-PadN12) -> /GND
- U2 pad P10: Net-(U2-PadK10) -> /1V8
- U2 pad P12: Net-(U2-PadK10) -> /1V8
- U2 pad P6: unconnected-(U2-PadP6) -> /FPGA/FPGA_DONE
- U2 pad P7: unconnected-(U2-PadP7) -> /1V8
- U2 pad P8: Net-(U2-PadK10) -> /1V8
- U2 pad R11: Net-(U2-PadK10) -> /1V8
- U2 pad R5: /1V8 -> /1V8_IO
- U2 pad R9: Net-(U2-PadK10) -> /1V8
- U2 pad T12: /1V8 -> /1V8_IO
- U2 pad T2: /1V8 -> /1V8_IO
- U2 pad U9: /1V8 -> /1V8_IO
- U2 pad V6: /1V8 -> /1V8_IO
- U2 pad W13: /1V8 -> /1V8_IO
- U2 pad W3: /1V8 -> /1V8_IO
- U2 pad Y10: /1V8 -> /1V8_IO
- U3 pad B1: unconnected-(U3-PadB1) -> /FPGA/QDR SRAM/QDR_Q27
- U3 pad B10: unconnected-(U3-PadB10) -> /FPGA/QDR SRAM/QDR_Q17
- U3 pad B11: unconnected-(U3-PadB11) -> /FPGA/QDR SRAM/QDR_Q8
- U3 pad B2: unconnected-(U3-PadB2) -> /FPGA/QDR SRAM/QDR_Q18
- U3 pad C10: unconnected-(U3-PadC10) -> /FPGA/QDR SRAM/QDR_Q7
- U3 pad C2: unconnected-(U3-PadC2) -> /FPGA/QDR SRAM/QDR_Q28
- U3 pad D3: unconnected-(U3-PadD3) -> /FPGA/QDR SRAM/QDR_Q19
- U3 pad D9: unconnected-(U3-PadD9) -> /FPGA/QDR SRAM/QDR_Q16
- U3 pad E1: unconnected-(U3-PadE1) -> /FPGA/QDR SRAM/QDR_Q29
- U3 pad E11: unconnected-(U3-PadE11) -> /FPGA/QDR SRAM/QDR_Q6
- U3 pad E3: unconnected-(U3-PadE3) -> /FPGA/QDR SRAM/QDR_Q20
- U3 pad E9: unconnected-(U3-PadE9) -> /FPGA/QDR SRAM/QDR_Q15
- U3 pad F1: unconnected-(U3-PadF1) -> /FPGA/QDR SRAM/QDR_Q30
- U3 pad F10: unconnected-(U3-PadF10) -> /FPGA/QDR SRAM/QDR_Q14
- U3 pad F11: unconnected-(U3-PadF11) -> /FPGA/QDR SRAM/QDR_Q5
- U3 pad F2: unconnected-(U3-PadF2) -> /FPGA/QDR SRAM/QDR_Q21
- U3 pad G3: unconnected-(U3-PadG3) -> /FPGA/QDR SRAM/QDR_Q22
- U3 pad G9: unconnected-(U3-PadG9) -> /FPGA/QDR SRAM/QDR_Q13
- U3 pad H1: unconnected-(U3-PadH1) -> /1V8_IO
- U3 pad H10: unconnected-(U3-PadH10) -> /QDR_VREF
- U3 pad H11: unconnected-(U3-PadH11) -> Net-(U3-PadH11)
- U3 pad H2: unconnected-(U3-PadH2) -> /QDR_VREF
- U3 pad J10: unconnected-(U3-PadJ10) -> /FPGA/QDR SRAM/QDR_Q4
- U3 pad J2: unconnected-(U3-PadJ2) -> /FPGA/QDR SRAM/QDR_Q31
- U3 pad K1: unconnected-(U3-PadK1) -> /FPGA/QDR SRAM/QDR_Q32
- U3 pad K11: unconnected-(U3-PadK11) -> /FPGA/QDR SRAM/QDR_Q3
- U3 pad K3: unconnected-(U3-PadK3) -> /FPGA/QDR SRAM/QDR_Q23
- U3 pad K9: unconnected-(U3-PadK9) -> /FPGA/QDR SRAM/QDR_Q12
- U3 pad L1: unconnected-(U3-PadL1) -> /FPGA/QDR SRAM/QDR_Q33
- U3 pad L10: unconnected-(U3-PadL10) -> /FPGA/QDR SRAM/QDR_Q11
- U3 pad L11: unconnected-(U3-PadL11) -> /FPGA/QDR SRAM/QDR_Q2
- U3 pad L2: unconnected-(U3-PadL2) -> /FPGA/QDR SRAM/QDR_Q24
- U3 pad M10: unconnected-(U3-PadM10) -> /FPGA/QDR SRAM/QDR_Q1
- U3 pad M2: unconnected-(U3-PadM2) -> /FPGA/QDR SRAM/QDR_Q34
- U3 pad N3: unconnected-(U3-PadN3) -> /FPGA/QDR SRAM/QDR_Q25
- U3 pad N9: unconnected-(U3-PadN9) -> /FPGA/QDR SRAM/QDR_Q10
- U3 pad P1: unconnected-(U3-PadP1) -> /FPGA/QDR SRAM/QDR_Q35
- U3 pad P11: unconnected-(U3-PadP11) -> /FPGA/QDR SRAM/QDR_Q0
- U3 pad P3: unconnected-(U3-PadP3) -> /FPGA/QDR SRAM/QDR_Q26
- U3 pad P9: unconnected-(U3-PadP9) -> /FPGA/QDR SRAM/QDR_Q9
- U3 pad R2: unconnected-(U3-PadR2) -> /GND
- U3 pad R6: unconnected-(U3-PadR6) -> /FPGA/QDR SRAM/QDR_ODT
